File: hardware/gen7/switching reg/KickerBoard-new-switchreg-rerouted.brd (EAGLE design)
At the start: 143.9 x 141.8 mm, 224 parts, among them IC1 LM2678S, Q1 IXFT94N30P3, Q2 IXFT94N30P3

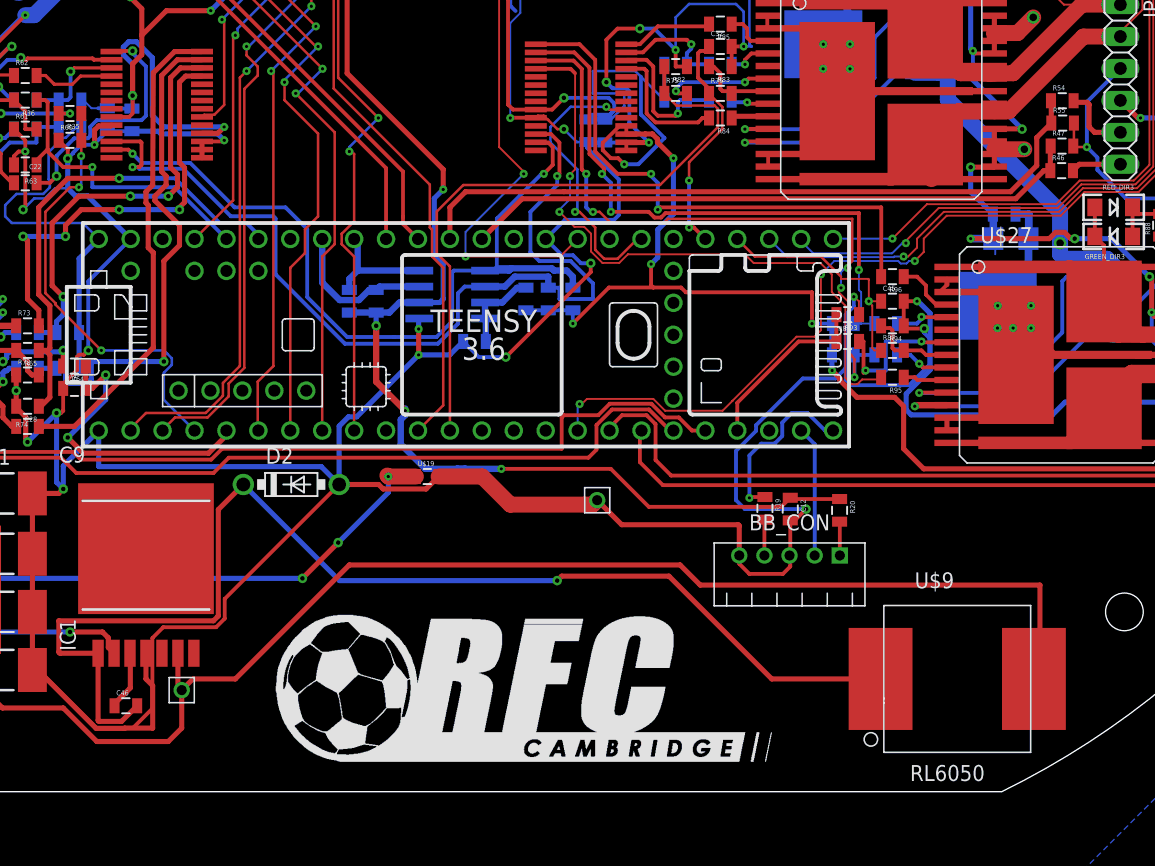
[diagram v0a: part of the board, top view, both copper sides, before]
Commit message: Changing to 3.3V
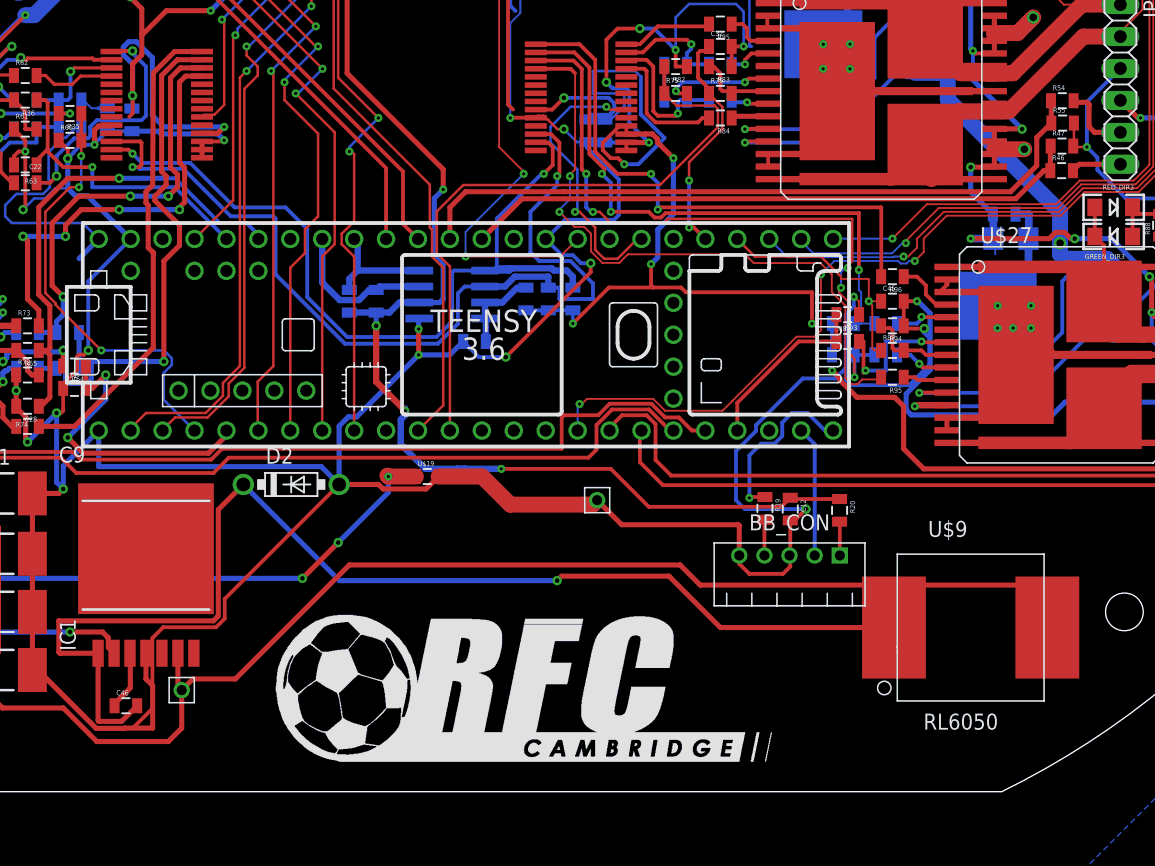
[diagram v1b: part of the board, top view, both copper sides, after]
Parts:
- moved U$9 4.23 mm to (110.8, 16.5)
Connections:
- net 3.3V: now also C35.1, C36.1, C37.1, C38.1, R41.2, R42.2, R69.2, R70.2, R80.2, R81.2, R91.2, R92.2, U$17.9, U$21.9
- net 5V: no longer C35.1, C36.1, C37.1, C38.1, R41.2, R42.2, R69.2, R70.2, R80.2, R81.2, R91.2, R92.2, U$17.9, U$21.9
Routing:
- net 5V: track 374.9 -> 328.6 mm, vias 21 -> 20
- net 3.3V: track 297.0 -> 320.3 mm, vias 14 -> 15
- net N$73: track 123.9 -> 119.9 mm
- net N$74: track 96.2 -> 95.6 mm

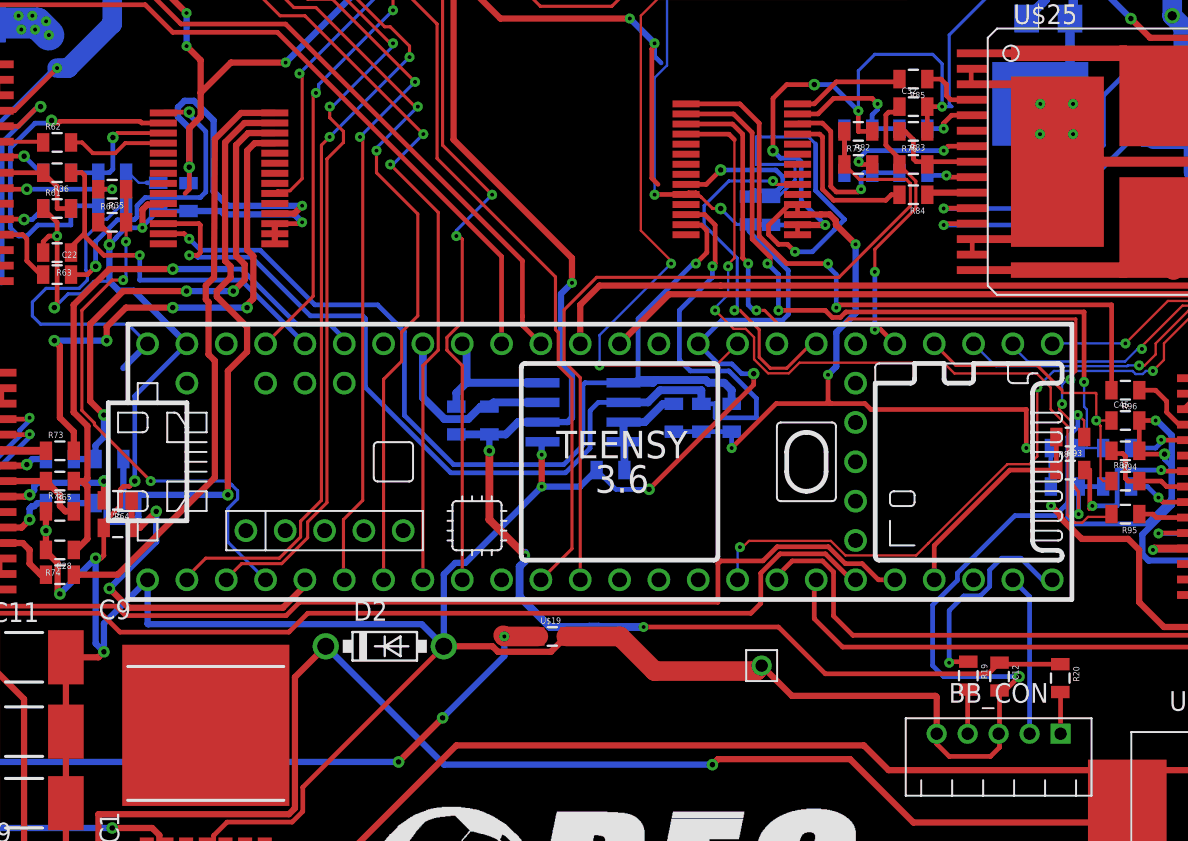
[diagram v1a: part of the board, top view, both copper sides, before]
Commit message: updating 3.3v wiring
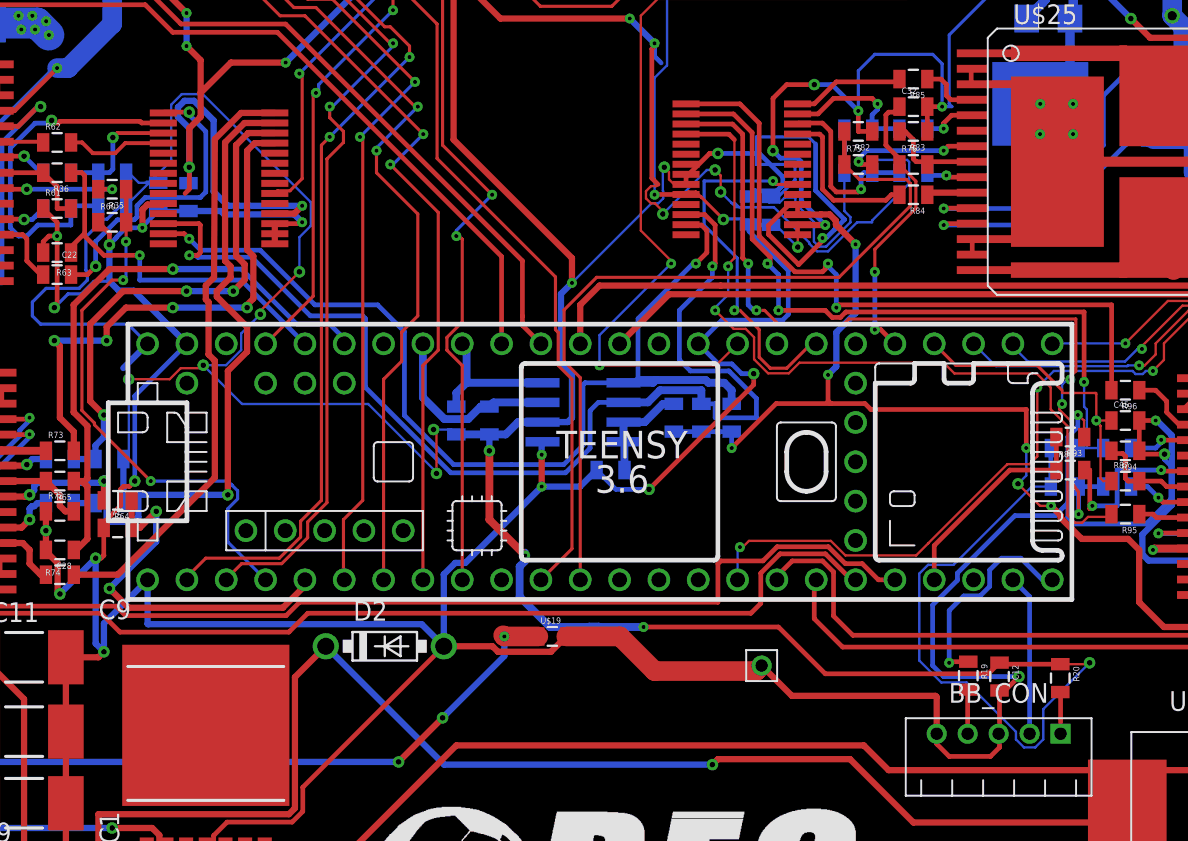
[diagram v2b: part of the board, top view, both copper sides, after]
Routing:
- net 3.3V: track 320.3 -> 450.1 mm, vias 15 -> 23
- net 5V: track 328.6 -> 366.1 mm, vias 20 -> 24
- net INT2: track 23.0 -> 24.0 mm
- net INA_3: track 44.1 -> 44.7 mm
- net GND: track 823.5 -> 823.8 mm, vias 49 -> 50
